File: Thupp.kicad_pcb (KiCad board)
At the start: 2 copper layers, 42 parts

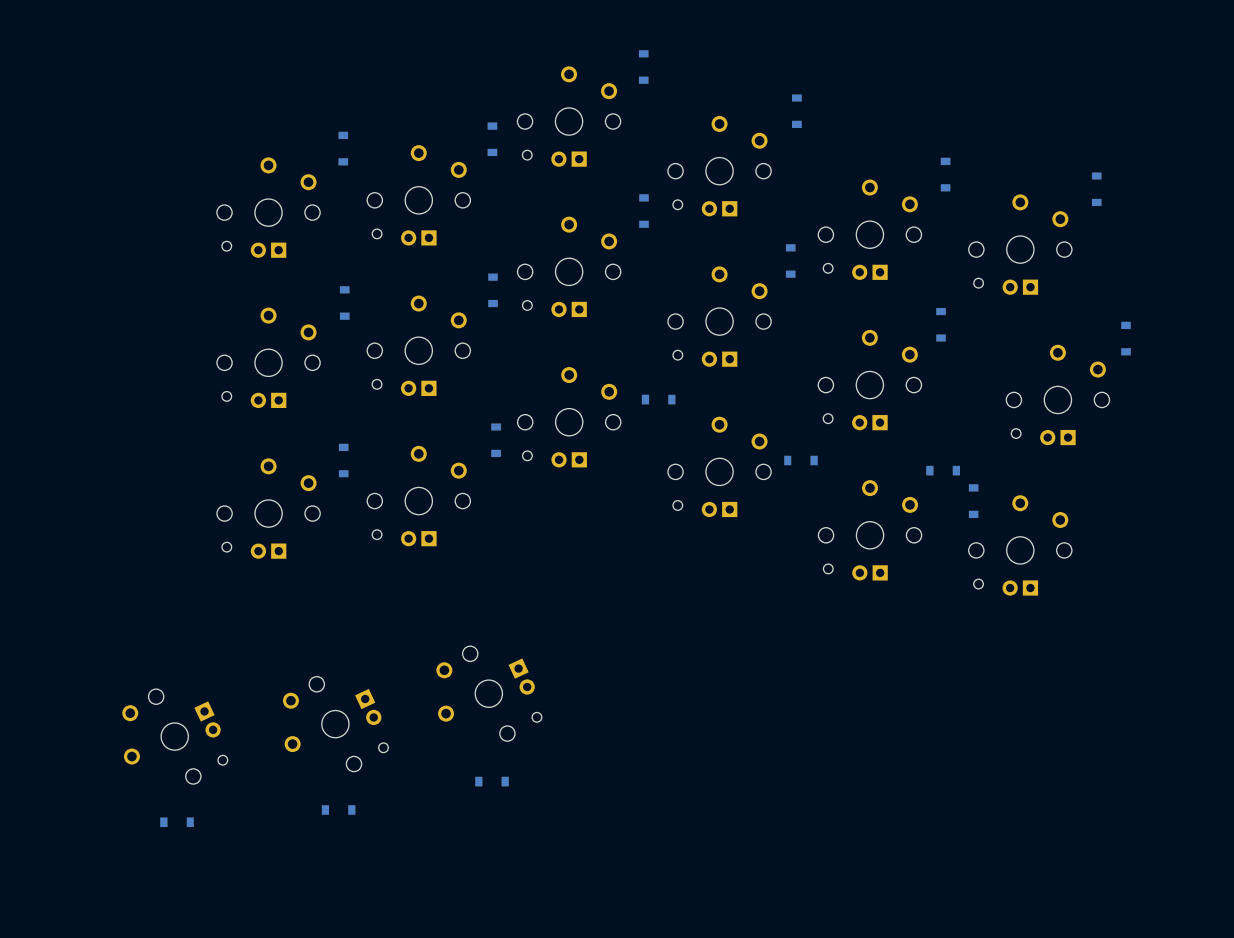
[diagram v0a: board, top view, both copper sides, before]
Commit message: most routing complete
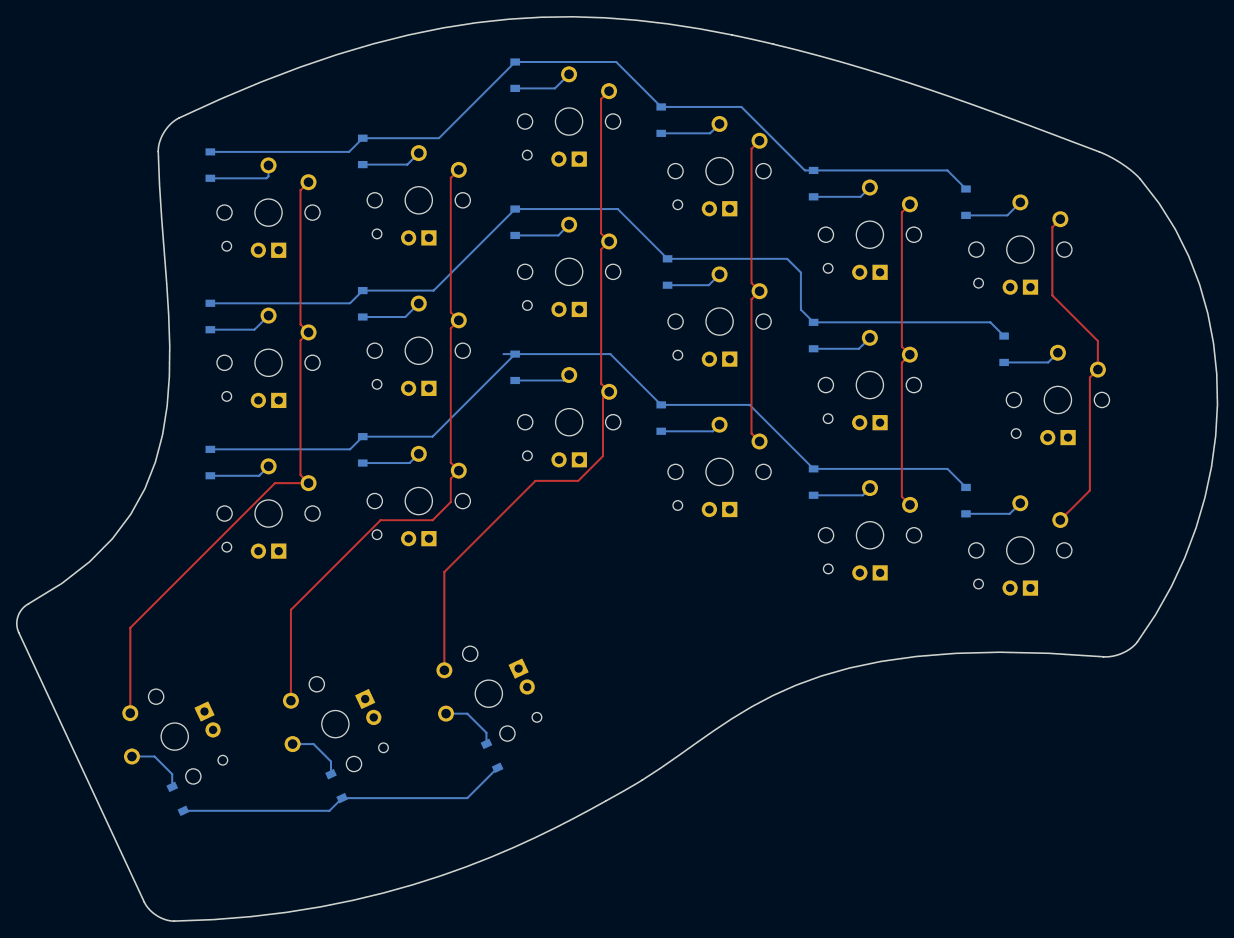
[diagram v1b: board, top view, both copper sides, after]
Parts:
- moved D11 18.4 mm to (78.6, 59.5), turned to 270 degrees
- moved D15 18.2 mm to (96.8, 65.8), turned to 270 degrees
- moved D13 17.0 mm to (96.8, 28.6)
- moved D2 16.9 mm to (40.5, 53.1)
- moved D1 16.7 mm to (40.5, 34.2)
- moved D7 16.7 mm to (59.5, 69.8)
- moved D3 16.7 mm to (40.5, 71.4)
- moved D16 16.5 mm to (115.9, 36.5)
- moved D19 16.4 mm to (134.9, 38.8)
- moved D6 16.4 mm to (59.5, 51.5)
- moved D5 16.3 mm to (59.5, 32.5)
- moved D18 16.3 mm to (115.9, 73.8), turned to 270 degrees
- moved D10 16.2 mm to (78.6, 41.3)
- moved D9 16.1 mm to (78.6, 23.0)
- moved D17 16.0 mm to (115.9, 55.5)
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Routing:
- net ROW2: track 0.00 -> 221.1 mm
- net ROW0: track 0.00 -> 105.7 mm
- net COL2: track 0.00 -> 85.7 mm
- net COL1: track 0.00 -> 80.5 mm
- net COL0: track 0.00 -> 79.7 mm
- net COL5: track 0.00 -> 42.3 mm
- net ROW3: track 0.00 -> 41.5 mm
- net COL3: track 0.00 -> 39.2 mm
- net COL4: track 0.00 -> 39.2 mm
- net Net-(D1-Pad2): track 0.00 -> 8.73 mm
- net Net-(D2-Pad2): track 0.00 -> 8.00 mm
- net Net-(D13-Pad2): track 0.00 -> 7.78 mm
- net Net-(D3-Pad2): track 0.00 -> 7.77 mm
- net Net-(D6-Pad2): track 0.00 -> 7.70 mm
- net Net-(D15-Pad2): track 0.00 -> 7.64 mm
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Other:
- board outline added: 150.1 x 113 mm
